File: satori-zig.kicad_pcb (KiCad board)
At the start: 2 copper layers, 70 x 25 mm, 8 parts

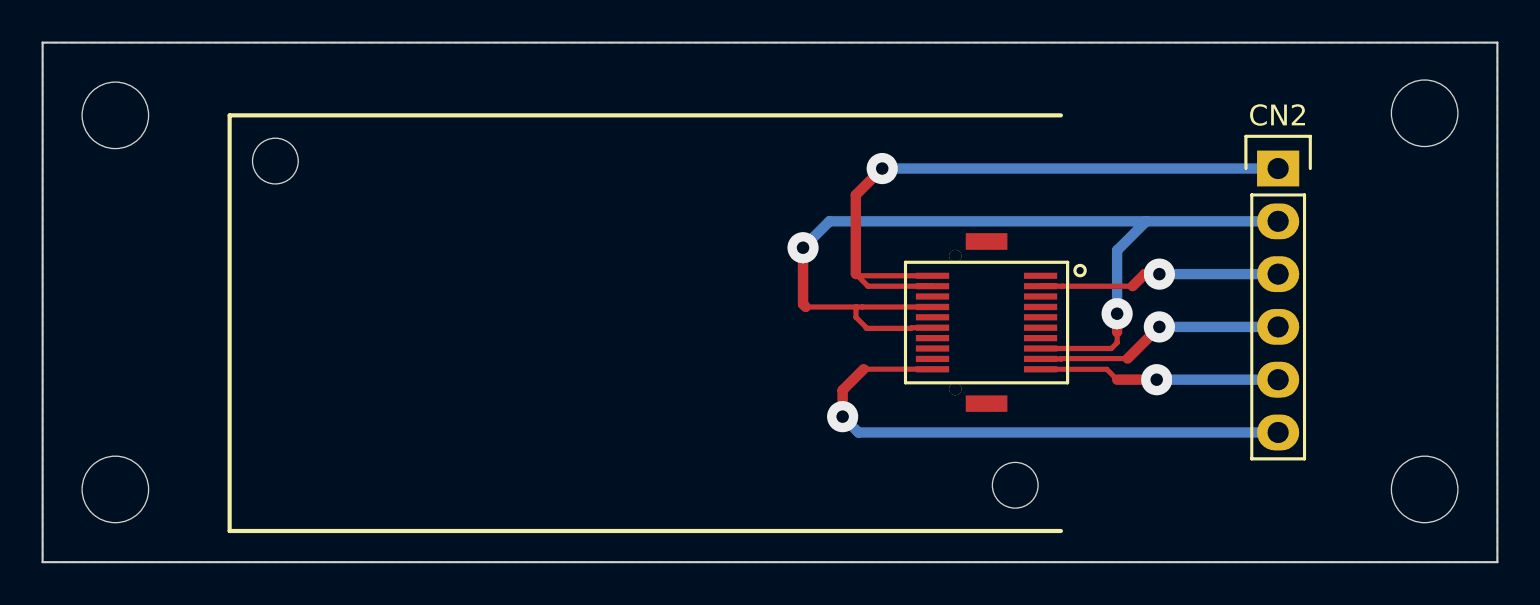
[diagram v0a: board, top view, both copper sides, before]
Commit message: Remove hatching
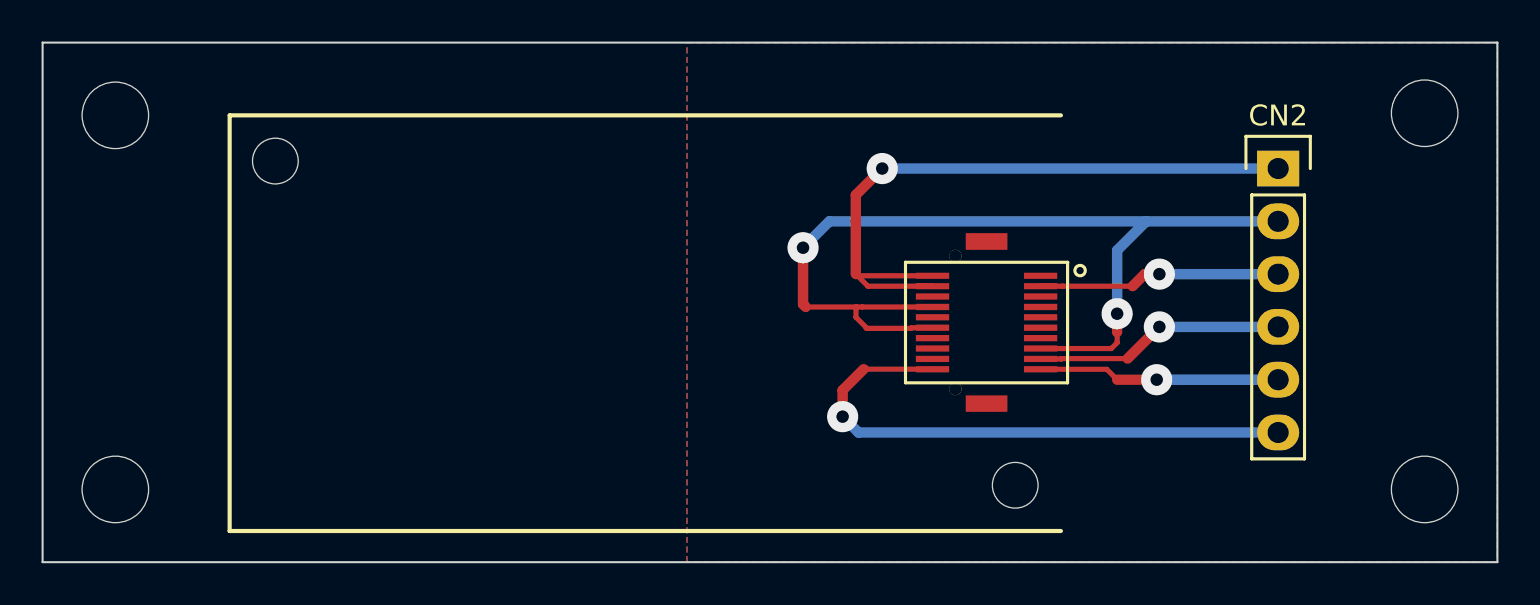
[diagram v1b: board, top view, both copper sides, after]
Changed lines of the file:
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@@
     (trace_clearance 0.2)
     (zone_clearance 0.508)
-    (zone_45_only no)
+    (zone_45_only yes)
     (trace_min 0.2)
     (segment_width 0.2)
@@
   (segment (start 150.495 110.998) (end 150.495 109.728) (width 0.5) (layer F.Cu) (net 17))
   (segment (start 154.812 108.712) (end 154.82 108.72) (width 0.25) (layer F.Cu) (net 17))
-  (zone (net 0) (net_name "") (layer F.Mask) (hatch full 0.508)
-    (connect_pads (clearance 0.508))
-    (min_thickness 0.254)
-    (fill yes (arc_segments 16) (thermal_gap 0.508) (thermal_bridge_width 0.508))
-    (polygon
-      (pts
-        (xy 159 109) (xy 156 109) (xy 156 104) (xy 159 104)
-      )
-    )
-  )
   (zone (net 6) (net_name GND) (layer B.Cu) (hatch edge 0.508)
     (connect_pads (clearance 0.508))
@@
     (polygon
       (pts
-        (xy 182 118) (xy 182 93) (xy 112 93) (xy 112 118)
+        (xy 182 118) (xy 143 118) (xy 143 93) (xy 182 93)
       )
     )
@@
     (polygon
       (pts
-        (xy 182 118) (xy 182 93) (xy 112 93) (xy 112 118)
+        (xy 182 118) (xy 143 118) (xy 143 93) (xy 182 93)
       )
     )
